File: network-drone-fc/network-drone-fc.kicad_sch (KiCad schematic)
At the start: 0 parts

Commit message: Schematic: complete MCU box
ESP32-S3FN8 with decoupling and VDD3P3 LC filter, EN RC reset, BOOT button,
40 MHz crystal, RF pi network to U.FL (shunts DNP), USB-C with ESD and
VBUS diode, status LEDs, UART test pads, and labels on all signal pins.
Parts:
- added C1, C2, C7, C8, C9: 0.1uF, symbol Device:C
- added C10, C11, C3, C5: 1uF, symbol Device:C
- added C12, C13: 15pF, symbol Device:C
- added C14, C15: DNP, symbol Device:C
- added C4: 10uF, symbol Device:C
- added C6: 10nF, symbol Device:C
- added D1: B5819W, symbol Device:D_Schottky
- added D2: RED, symbol Device:LED
- added D3: GREEN, symbol Device:LED
- added D4: YELLOW, symbol Device:LED
- added J1: U.FL-R-SMT-1, tar_fc:RF-SMD_FRF05002-JSS103M, symbol tar_fc:U.FL-R-SMT-1
- added J2: TYPE-C 16PIN 2MD, tar_fc:USB-C-SMD_TYPE-C-16PIN-2MD-073, symbol tar_fc:TYPE-C16PIN2MD
- added L1: 2.0nH, symbol Device:L
- added R1: 10k, symbol Device:R
- added R2, R3: 0, symbol Device:R
- added R4, R5: 5.1k, symbol Device:R
- added R6, R8: 1k, symbol Device:R
- added R7: 470, symbol Device:R
- added SW1: RESET, symbol Switch:SW_Push
- added SW2: BOOT, symbol Switch:SW_Push
- added TP1, TP2: TestPoint, symbol Connector:TestPoint
- added U1: ESP32-S3FN8, Package_DFN_QFN:QFN-56-1EP_7x7mm_P0.4mm_EP4x4mm, symbol MCU_Espressif:ESP32-S3
- added U2: USBLC6-2SC6, Package_TO_SOT_SMD:SOT-23-6, symbol Power_Protection:USBLC6-2SC6
- added X1: Q22FA12800101, tar_fc:CRYSTAL-SMD_4P-L2.0-W1.6-BL, symbol tar_fc:Q22FA12800101
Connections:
- new net: J2.A5 (CC1), R5.1
- new net: C14.1, J1.1 (SIG), R3.1
- new net: C10.1, C9.1, U1.29 (VDD_SPI)
- new net: D4.2 (A), R8.2
- new net: J2.B5 (CC2), R4.1
- new net: C11.1, R1.2, SW1.2, U1.4 (CHIP_PU)
- new net: C1.1, L1.2, U1.2 (VDD3P3), U1.3 (VDD3P3)
- new net: TP1.1, U1.49 (U0TXD)
- new net: SW2.2, U1.5 (GPIO0)
- new net: TP2.1, U1.50 (U0RXD)
- new net: C12.1, R2.2, X1.1 (OSC1)
- new net: D2.2 (A), R6.2
- new net: D3.2 (A), R7.2
- new net +3V3: C2.1, C3.1, C4.1, C5.1, C6.1, C7.1, C8.1, L1.1, R1.1, R6.1, U1.20 (VDD3P3_RTC), U1.46 (VDD3P3_CPU), U1.55 (VDDA), U1.56 (VDDA)
- new net +5V: D1.1 (K)
- new net Antenna: C15.1, R3.2, U1.1 (LNA_IN)
- new net BNO_CS: U1.19 (GPIO14)
- new net BNO_INTR: U1.22 (XTAL_32K_N)
- new net BNO_RST: U1.23 (GPIO17)
- new net BNO_WAKE: U1.24 (GPIO18)
- new net D+: J2.A6 (Dp1), J2.B6 (Dp2), U2.1 (I/O1)
- new net D-: J2.A7 (Dn1), J2.B7 (Dn2), U2.3 (I/O2)
- new net ESC_CUR: U1.7 (GPIO2)
- new net ESC_TELEM: U1.13 (GPIO8)
- new net GND: C1.2, C10.2, C11.2, C12.2, C13.2, C14.2, C15.2, C2.2, C3.2, C4.2, C5.2, C6.2, C7.2, C8.2, C9.2, D2.1 (K), D3.1 (K), D4.1 (K), J1.2 (GND), J1.3 (GND), J2.13 (EH), J2.14 (EH), J2.A1B12 (GND), J2.B1A12 (GND), R4.2, R5.2, SW1.1, SW2.1, U1.57 (GND), U2.2 (GND), X1.2, X1.4
- new net GPS_RX: U1.41 (GPIO36)
- new net GPS_TX: U1.40 (GPIO35)
- new net Green: R7.1, U1.37 (SPICLK_P)
- new net I2C_SCL: U1.39 (GPIO34)
- new net I2C_SDA: U1.38 (GPIO33)
- new net ICM_CS: U1.15 (GPIO10)
- new net ICM_INTR: U1.21 (XTAL_32K_P)
- new net MOTOR1: U1.9 (GPIO4)
- new net MOTOR2: U1.10 (GPIO5)
- new net MOTOR3: U1.11 (GPIO6)
- new net MOTOR4: U1.12 (GPIO7)
- new net SPI_MISO: U1.18 (GPIO13)
- new net SPI_MOSI: U1.16 (GPIO11)
- new net SPI_SCK: U1.17 (GPIO12)
- new net UART_RX: U1.43 (GPIO38)
- new net UART_TX: U1.42 (GPIO37)
- new net USB_DN: U1.25 (GPIO19/USB_D-), U2.4 (I/O2)
- new net USB_DP: U1.26 (GPIO20/USB_D+), U2.6 (I/O1)
- new net VBAT_SENSE: U1.6 (GPIO1)
- new net VBUS: D1.2 (A), J2.A4B9 (VBUS), J2.B4A9 (VBUS), U2.5 (VBUS)
- new net XTAL_N: C13.1, U1.53 (XTAL_N), X1.3 (OSC2)
- new net XTAL_P: R2.1, U1.54 (XTAL_P)
- new net Yellow: R8.1, U1.36 (SPICLK_N)
- no-connect marks 0 -> 18
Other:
- note added: "Antenna"
- note added: "Connectors"
- note added: "Crystal"
- note added: "Leds"
- note added: "MCU"
- note added: "Power"
- note added: "Sensors"
- note added: "USB"

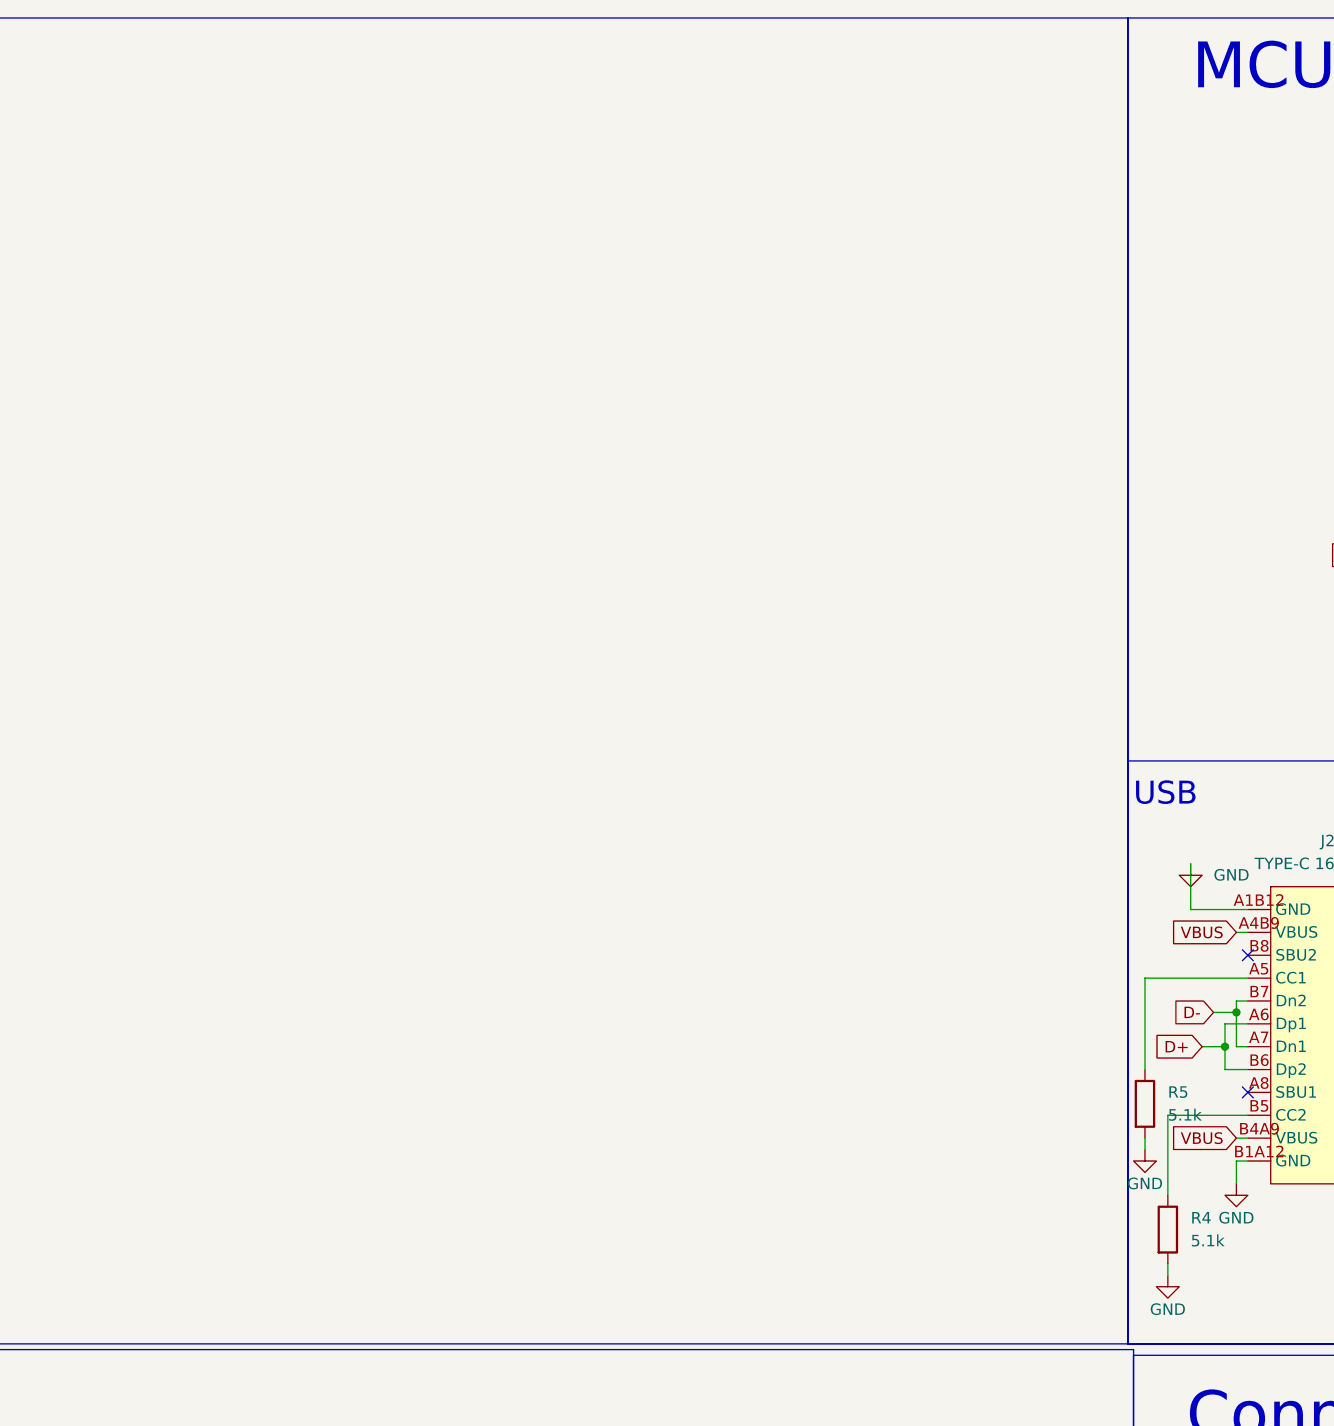
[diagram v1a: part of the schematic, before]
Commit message: Schematic: power box - SMAJ18A TVS, AP63205 5 V buck, dual 3.3 V LDOs
TLV75733 feeds the ESP32 rail (+3V3); low-noise TPS7A2033 feeds a separate
+3V3_SENS rail so radio TX bursts stay out of the IMU and barometer supply.
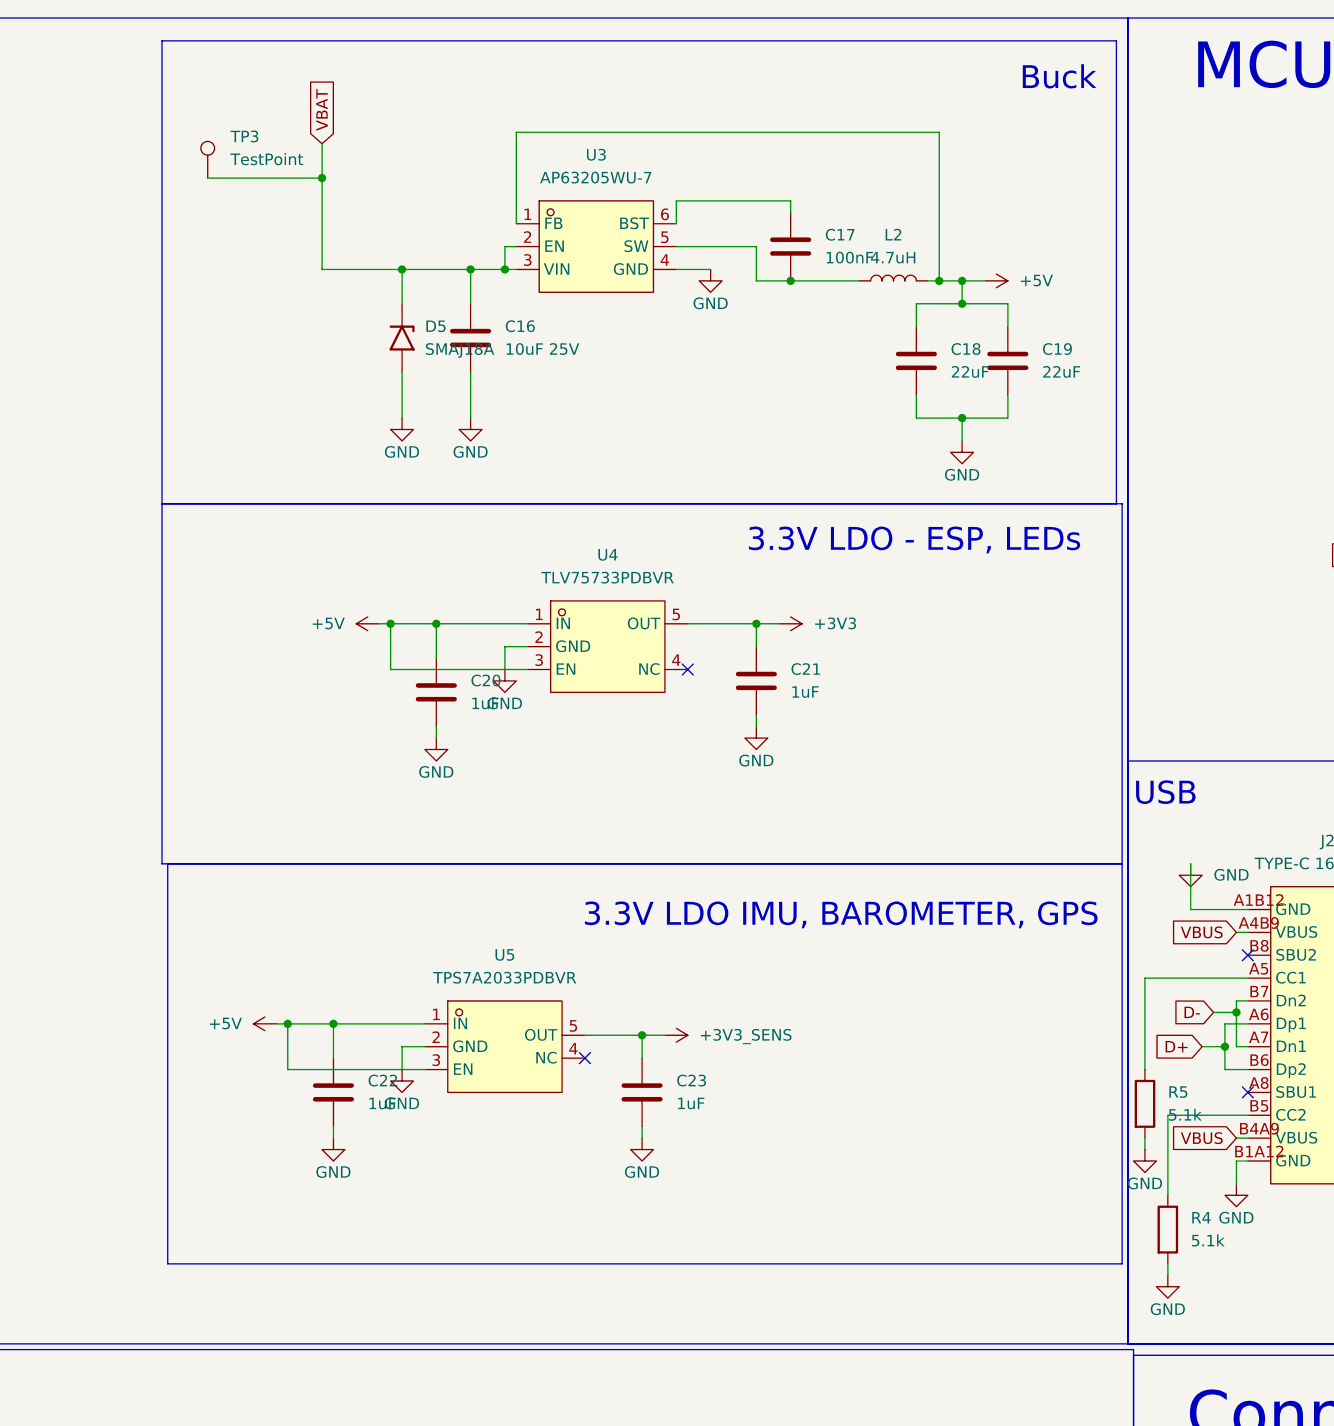
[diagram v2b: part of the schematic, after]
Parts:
- added C16: 10uF 25V, symbol Device:C
- added C17: 100nF, symbol Device:C
- added C18, C19: 22uF, symbol Device:C
- added C20, C21, C22, C23: 1uF, symbol Device:C
- added D5: SMAJ18A, Diode_SMD:D_SMA, symbol Diode:SMAJ18A
- added L2: 4.7uH, symbol Device:L
- added TP3: TestPoint, symbol Connector:TestPoint
- added U3: AP63205WU-7, tar_fc:TSOT-23-6_L2.9-W1.6-P0.95-LS2.8-BL, symbol tar_fc:AP63205WU-7
- added U4: TLV75733PDBVR, tar_fc:SOT-23-5_L2.9-W1.6-P0.95-LS2.8-BL, symbol tar_fc:TLV75733PDBVR
- added U5: TPS7A2033PDBVR, tar_fc:SOT-23-5_L2.9-W1.6-P0.95-LS2.8-BR, symbol tar_fc:TPS7A2033PDBVR
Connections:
- net +3V3: now also C21.1, U4.5 (OUT)
- net +5V: now also C18.1, C19.1, C20.1, C22.1, L2.2, U3.1 (FB), U4.1 (IN), U4.3 (EN), U5.1 (IN), U5.3 (EN)
- net GND: now also C16.2, C18.2, C19.2, C20.2, C21.2, C22.2, C23.2, D5.2 (A2), U3.4 (GND), U4.2 (GND), U5.2 (GND)
- new net: C17.2, L2.1, U3.5 (SW)
- new net: C17.1, U3.6 (BST)
- new net +3V3_SENS: C23.1, U5.5 (OUT)
- new net VBAT: C16.1, D5.1 (A1), TP3.1, U3.2 (EN), U3.3 (VIN)
- no-connect marks 18 -> 20
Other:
- note added: "3.3V LDO - ESP, LEDs"
- note added: "3.3V LDO IMU, BAROMETER, GPS"
- note added: "Buck"

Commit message: Schematic: battery sense divider (VBAT/11 to ADC1) and rail test points
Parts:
- added C24: 100nF, symbol Device:C
- added R10: 10k, symbol Device:R
- added R9: 100k, symbol Device:R
- added TP4, TP5, TP6: TestPoint, symbol Connector:TestPoint
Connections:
- net +3V3: now also TP5.1
- net +3V3_SENS: now also TP6.1
- net +5V: now also TP4.1
- net GND: now also C24.2, R10.2
- net VBAT: now also R9.1
- net VBAT_SENSE: now also C24.1, R10.1, R9.2
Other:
- note added: "Battery sense divider"
